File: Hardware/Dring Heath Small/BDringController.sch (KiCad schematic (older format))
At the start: 93 parts, among them J1 Module 1, J10 Module 3, J11 JTAG, J12 Shift Regs and Motor Drvs, J13 Module 4, J14 Module 5, J15 Micro_SD_Card, J16 Pin, J17 Pin, J18 Pin, J19 Pin, J2 Jumper, J20 Pin, J21 Pin, J22 AUX GPIO, J3 Motor, J4 Module 1, J5 Ext Mot Drv, J6 01x02, J7 THC_Display, J8 Module 2, J9 VMot, U1 ESP32_38p, U10 Y, U11 z, U12 A, U13 B, U14 C, U2 74LVC157A, U3 ESP32_38p, U4 TC1262-33, U5 74AHCT595, U6 74AHCT595, U7 74AHCT595, U8 74AHCT595, U9 X

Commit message: Routing
needs 2 Jumper wires 18v in and 15v
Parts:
- added C25: 100nf, Capacitor_SMD:C_0603_1608Metric_Pad1.08x0.95mm_HandSolder, symbol Device:C_Small
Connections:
- net +3V3: now also C25.2
- net GND: now also J6.2 (Pin_2), PS1.2 (-Vin), PS2.2 (-Vin), C25.1
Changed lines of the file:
@@
 $EndComp
 Wire Wire Line
-	11250 2850 11250 3350
-Wire Wire Line
 	11250 3350 11650 3350
-Connection ~ 11650 3350
 Wire Wire Line
 	9950 1950 9950 2450
@@
 	-1   0    0    1
 $EndComp
+$Comp
+L Device:C_Small C25
+U 1 1 6025EA04
+P 5450 1300
+F 0 "C25" V 5500 1050 50  0000 C CNN
+F 1 "100nf" V 5400 1050 50  0000 C CNN
+F 2 "Capacitor_SMD:C_0603_1608Metric_Pad1.08x0.95mm_HandSolder" H 5450 1300 50  0001 C CNN
+F 3 "~" H 5450 1300 50  0001 C CNN
+	1    5450 1300
+	0    -1   -1   0
+$EndComp
+Connection ~ 5350 1300
+Wire Wire Line
+	5550 1300 5900 1300
+Wire Wire Line
+	5900 1300 5900 1400
+Wire Wire Line
+	5900 1400 6050 1400
+Connection ~ 6050 1400
+Connection ~ 11650 3350
+Wire Wire Line
+	11250 2850 11250 3350
+$Comp
+L power:GND #PWR0106
+U 1 1 605E21DB
+P 6250 7100
+F 0 "#PWR0106" H 6250 6850 50  0001 C CNN
+F 1 "GND" H 6255 6927 50  0000 C CNN
+F 2 "" H 6250 7100 50  0001 C CNN
+F 3 "" H 6250 7100 50  0001 C CNN
+	1    6250 7100
+	1    0    0    -1
+$EndComp
+Wire Wire Line
+	6100 7100 6250 7100
 Wire Bus Line
 	9500 1650 9500 5450

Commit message: Main and Module Boards Routed
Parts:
- removed J11: JTAG, Connector_PinHeader_2.54mm:PinHeader_2x05_P2.54mm_Horizontal, symbol Connector:Conn_ARM_JTAG_SWD_10
- added H10, H11, H8, H9: ~, Connector_Pin:Pin_D0.9mm_L10.0mm_W2.4mm_FlatFork, symbol Mechanical:MountingHole_Pad
- renumbered C6 to C1, C14 to C10, C15 to C11, C16 to C12, C17 to C13, C18 to C14, C1 to C15, C19 to C16, C2 to C17, C20 to C18, C3 to C19, C25 to C2, C21 to C20, C4 to C21, C5 to C23, C23 to C24, C24 to C25, C7 to C3, C8 to C4, C9 to C5, C10 to C6, C11 to C7, C12 to C8, C13 to C9, J22 to J1, J8 to J10, J9 to J11, J10 to J12, J12 to J13, J13 to J14, J14 to J15, J15 to J16, J16 to J17, J17 to J18, J18 to J19, J23 to J2, J19 to J20, J20 to J21, J21 to J22, J1 to J3, J2 to J4, J3 to J5, J4 to J6, J5 to J7, J6 to J8, J7 to J9, R21 to R10, R22 to R11, R23 to R12, R16 to R5, R17 to R6, R18 to R7, R19 to R8, R20 to R9
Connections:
- net +15V: now also H11.1
- net at J8.1 (Pin_1), PS1.1 (+Vin), PS2.1 (+Vin): now also H9.1
- no-connect marks 39 -> 41
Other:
- moved on the sheet: C5, C8, D1, J13, U3

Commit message: Pin changes
Put RJ45 connector on Jtag module for more IO put Pot on Torch module to
adjust Plasma voltage
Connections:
- net TCH_V_IO36: now reaches U1.22 (IO36)
- net TCH_V_IO36: now also J12.10 (7)
- net TCHIO17: no longer names the net of U1.9 (IO17)
- net TCHIO17: no longer J12.10 (7)
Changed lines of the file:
@@
 TCHIO21
 Text GLabel 8150 8850 1    39   BiDi ~ 8
-TCHIO17
-Text GLabel 4800 1500 2    39   BiDi ~ 8
-TCHIO22
+TCH_V_IO36
 Text GLabel 4800 1800 2    39   BiDi ~ 8
 TCHIO21
-Text GLabel 4800 2300 2    39   BiDi ~ 8
-TCHIO17
 $Comp
 L power:GND #PWR09
@@
 Wire Wire Line
 	4100 3800 4100 4000
-NoConn ~ 4000 1500
 Text GLabel 4000 1900 0    39   Input ~ 0
 TorchTrigger
@@
 NoConn ~ 3500 5350
 NoConn ~ 3500 5450
+Text GLabel 4000 1500 0    39   BiDi ~ 8
+TCH_V_IO36
+Text GLabel 4800 1500 2    39   BiDi ~ 8
+TCHIO22
+NoConn ~ 4800 2300
 Wire Bus Line
 	9500 1650 9500 5450

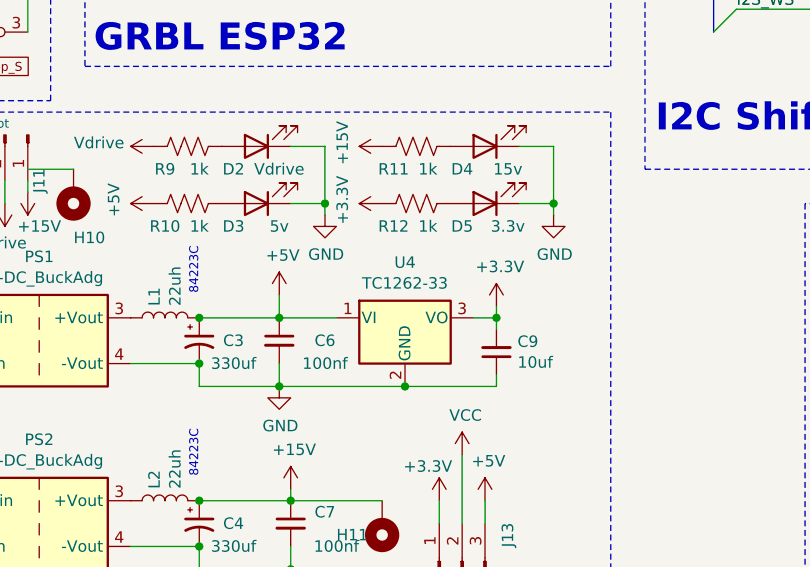
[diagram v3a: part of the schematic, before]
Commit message: Change to BOM
Shifted a few tracks changed 3.3v reg to 1A
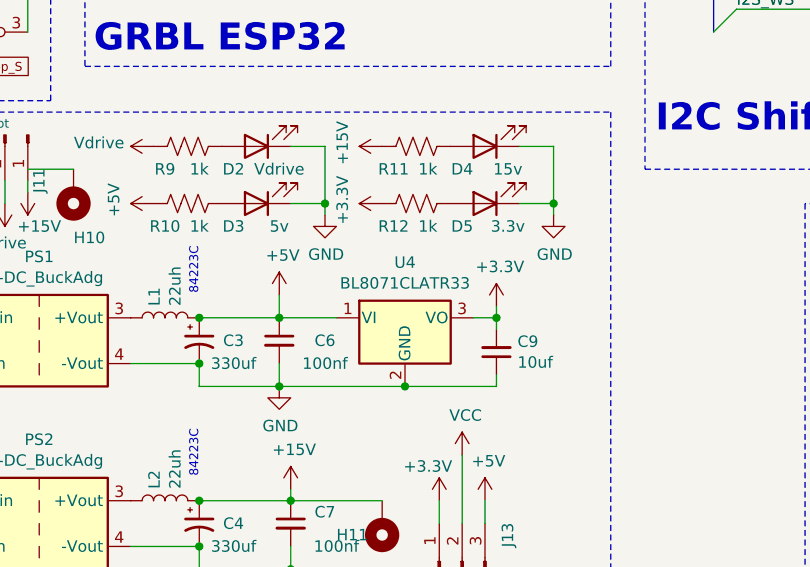
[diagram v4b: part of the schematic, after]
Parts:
- U4: value TC1262-33 -> BL8071CLATR33
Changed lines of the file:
@@
 P 8150 6700
 F 0 "U4" H 8150 6942 50  0000 C CNN
-F 1 "TC1262-33" H 8150 6851 50  0000 C CNN
+F 1 "BL8071CLATR33" H 8150 6851 50  0000 C CNN
 F 2 "Package_TO_SOT_SMD:SOT-223" H 8150 6925 50  0001 C CIN
 F 3 "http://ww1.microchip.com/downloads/en/DeviceDoc/21373C.pdf" H 8150 6400 50  0001 C CNN

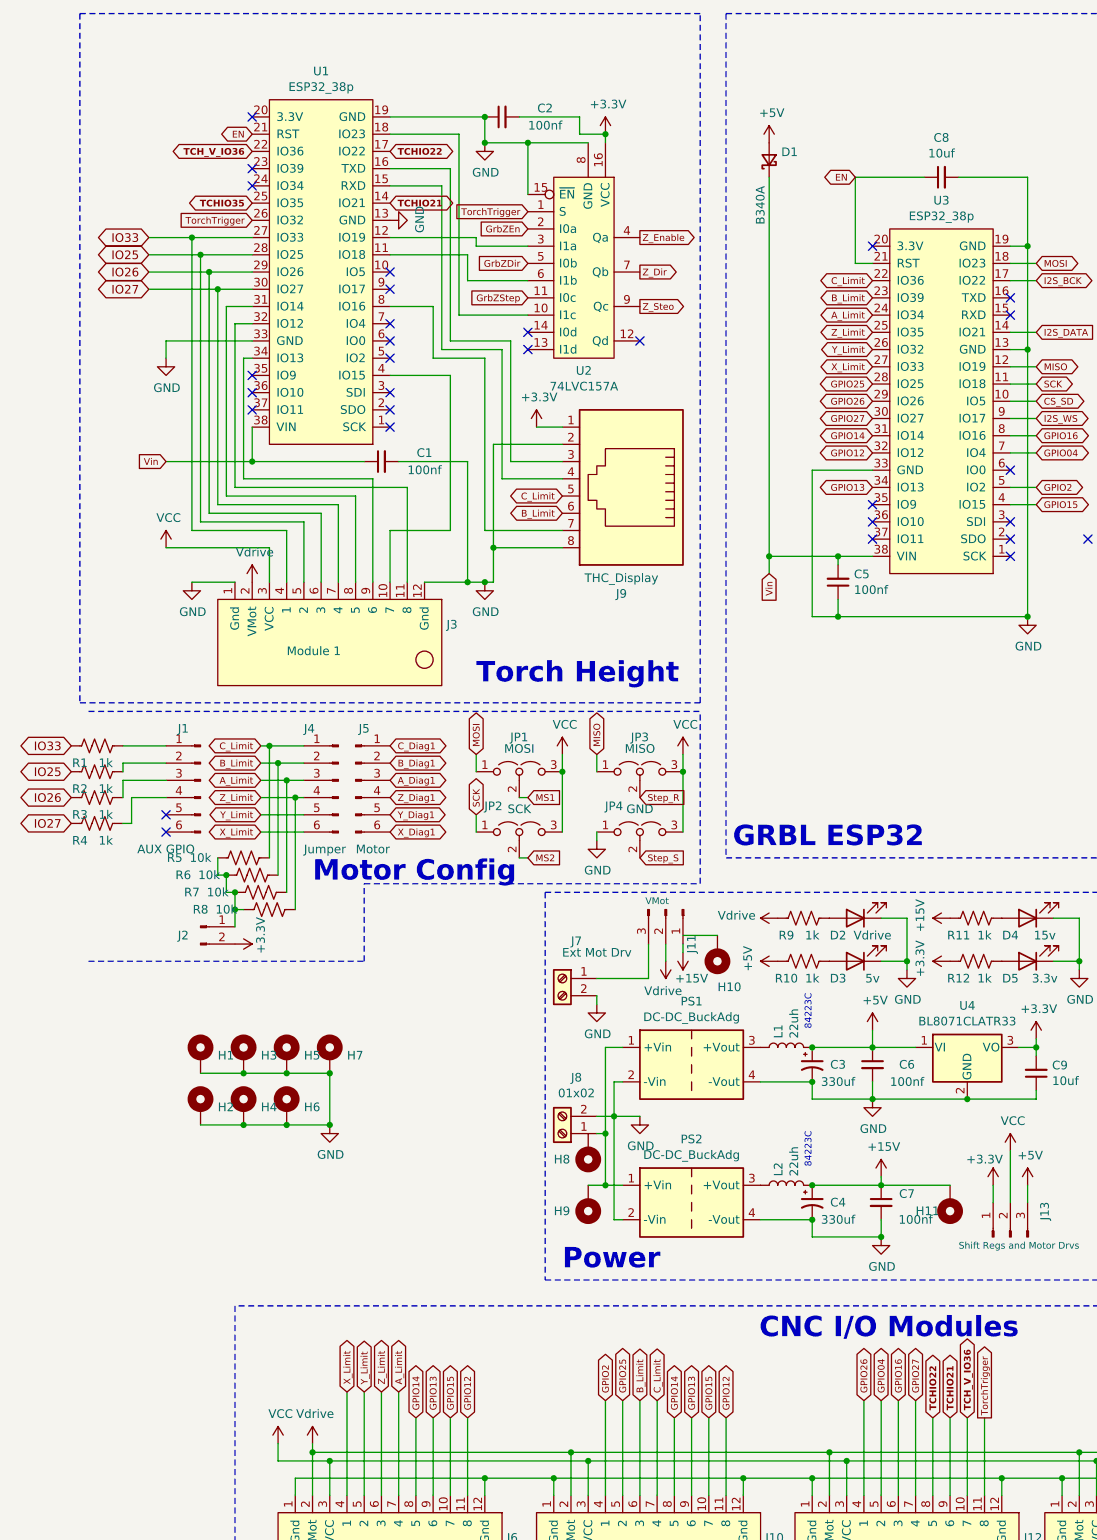
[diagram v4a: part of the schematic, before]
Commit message: Added external A/D ADS1115
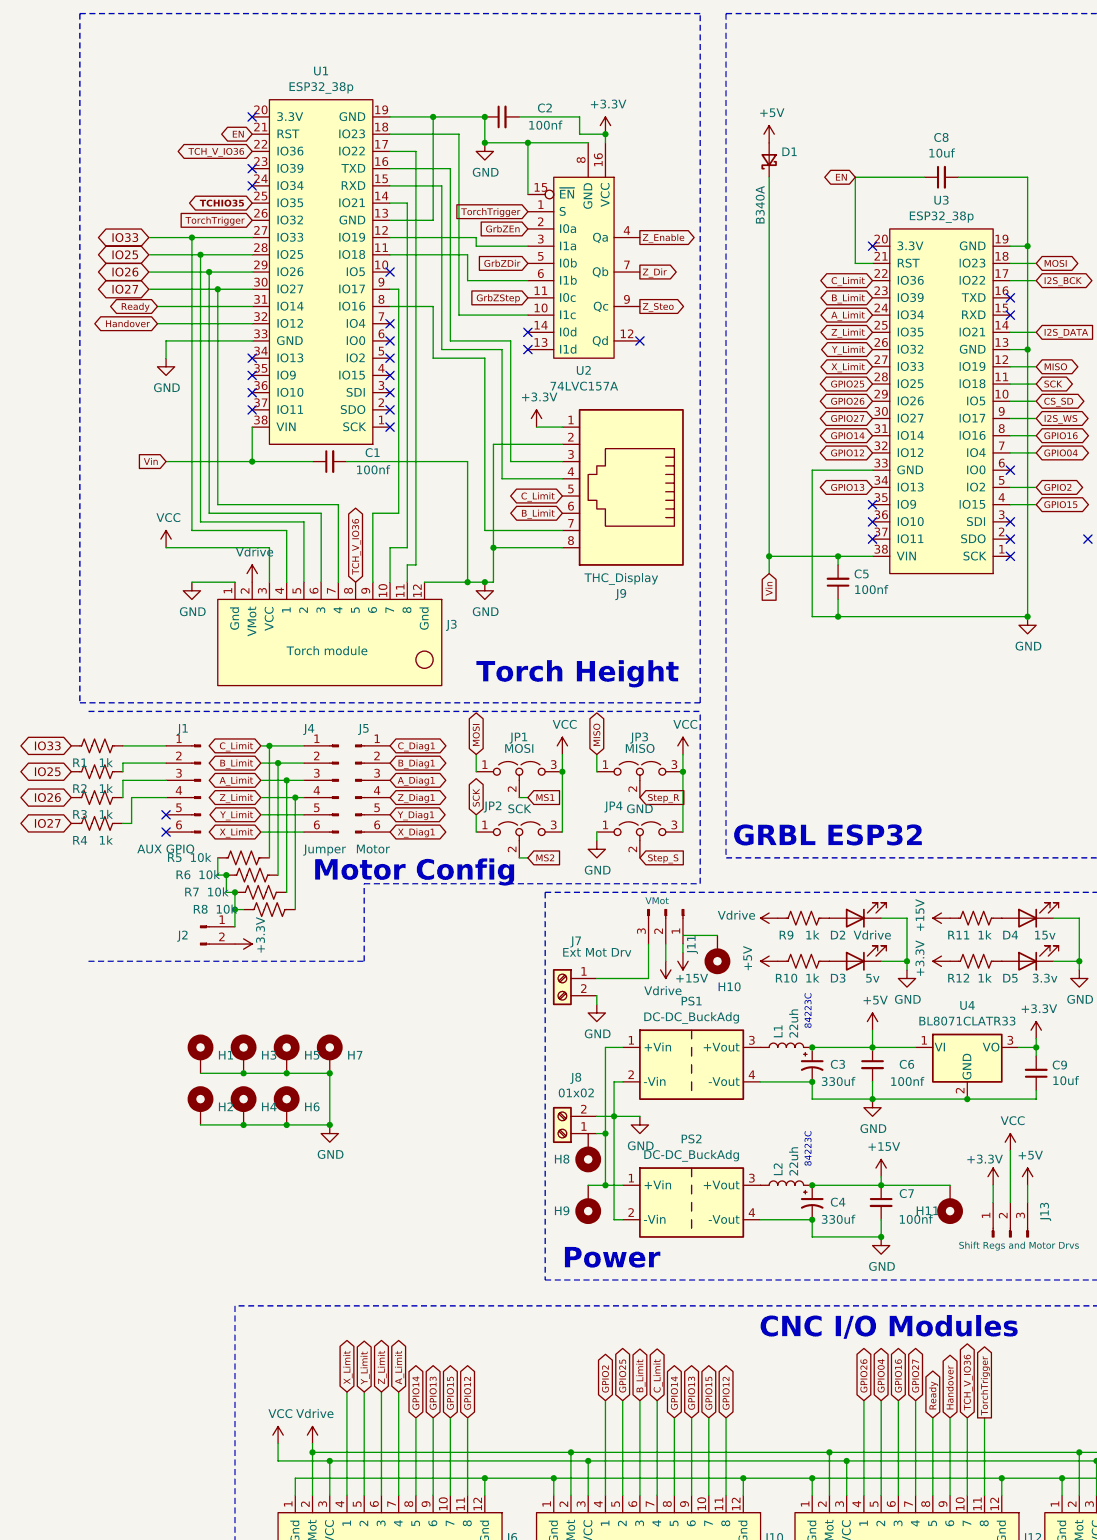
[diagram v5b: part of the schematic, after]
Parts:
- J3: value Module 1 -> Torch module
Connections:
- net TCH_V_IO36: now also J3.8 (5)
- net Ready: now reaches U1.31 (IO14)
- net Ready: now also J12.8 (5); no longer J3.8 (5)
- net at J3.11 (8): now also U1.17 (IO22); no longer U1.32 (IO12)
- net at U1.34 (IO13): no longer J3.9 (6)
- net at J3.10 (7): now also U1.14 (IO21); no longer U1.4 (IO15)
- net at U1.9 (IO17): now also J3.9 (6)
- net TCHIO21 renamed Handover
- net Handover: now also U1.32 (IO12); no longer U1.14 (IO21)
- removed net TCHIO22: J12.8 (5), U1.17 (IO22)
- no-connect marks 41 -> 42
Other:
- moved on the sheet: C1
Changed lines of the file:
@@
 P 4450 4350
 F 0 "J3" H 3772 4246 50  0000 R CNN
-F 1 "Module 1" H 4700 4400 50  0000 R CNN
+F 1 "Torch module" H 4700 4400 50  0000 R CNN
 F 2 "Connector_PinSocket_2.54mm:PinSocket_1x12_P2.54mm_Vertical" H 4350 4300 50  0001 C CNN
 F 3 "" H 4350 4300 50  0001 C CNN
@@
 	-1   0    0    1
 $EndComp
-Wire Wire Line
-	4000 2500 3900 2500
-Wire Wire Line
-	3900 2500 3900 3450
-Wire Wire Line
-	3900 3450 4900 3450
-Wire Wire Line
-	4900 3450 4900 4000
-Wire Wire Line
-	4800 3700 4800 4000
-Wire Wire Line
-	4000 2700 3950 2700
-Wire Wire Line
-	3950 2700 3950 3400
-Wire Wire Line
-	3950 3400 4700 3400
-Wire Wire Line
-	4700 3400 4700 4000
-Wire Wire Line
-	4000 2400 3850 2400
-Wire Wire Line
-	3850 2400 3850 3500
-Wire Wire Line
-	3850 3500 4600 3500
-Wire Wire Line
-	4600 3500 4600 4000
 Wire Wire Line
 	4000 2300 3800 2300
@@
 L Device:C_Small C1
 U 1 1 60B8E4F3
-P 4750 3300
-F 0 "C1" V 4800 3050 50  0000 C CNN
-F 1 "100nf" V 4700 3050 50  0000 C CNN
-F 2 "Capacitor_SMD:C_0603_1608Metric_Pad1.08x0.95mm_HandSolder" H 4750 3300 50  0001 C CNN
-F 3 "~" H 4750 3300 50  0001 C CNN
-	1    4750 3300
+P 4450 3300
+F 0 "C1" V 4500 3050 50  0000 C CNN
+F 1 "100nf" V 4400 3050 50  0000 C CNN
+F 2 "Capacitor_SMD:C_0603_1608Metric_Pad1.08x0.95mm_HandSolder" H 4450 3300 50  0001 C CNN
+F 3 "~" H 4450 3300 50  0001 C CNN
+	1    4450 3300
 	0    -1   -1   0
 $EndComp
@@
 Text GLabel 5600 2350 0    39   Input ~ 0
 GrbZStep
-Wire Wire Line
-	5150 2800 5150 3700
 NoConn ~ 4000 2800
 NoConn ~ 4000 2900
@@
 	3500 2600 3500 2700
 Wire Wire Line
-	4000 3300 4650 3300
+	4000 3300 4350 3300
 Wire Wire Line
 	3500 3300 4000 3300
@@
 	5000 4000 5250 4000
 Wire Wire Line
-	4800 1300 5350 1300
+	4800 1300 5050 1300
 Wire Wire Line
 	4800 1400 5200 1400
@@
 	4800 2400 5050 2400
 Wire Wire Line
-	4800 2800 5150 2800
-Wire Wire Line
-	4850 3300 5250 3300
-Wire Wire Line
-	4800 3700 5150 3700
+	4550 3300 5250 3300
 Wire Wire Line
 	5400 4000 5350 4000
 Connection ~ 5350 4000
-Text GLabel 7950 8850 1    39   BiDi ~ 8
-TCHIO22
-Text GLabel 8050 8850 1    39   BiDi ~ 8
-TCHIO21
-Text GLabel 8150 8850 1    39   BiDi ~ 8
+Text GLabel 7950 8850 1    39   BiDi ~ 0
+Ready
+Text GLabel 8050 8850 1    39   BiDi ~ 0
+Handover
+Text GLabel 8150 8850 1    39   BiDi ~ 0
 TCH_V_IO36
-Text GLabel 4800 1800 2    39   BiDi ~ 8
-TCHIO21
-$Comp
-L power:GND #PWR09
-U 1 1 642F7395
-P 4800 1900
-F 0 "#PWR09" H 4800 1650 50  0001 C CNN
-F 1 "GND" H 4805 1727 50  0000 C CNN
-F 2 "" H 4800 1900 50  0001 C CNN
-F 3 "" H 4800 1900 50  0001 C CNN
-	1    4800 1900
-	0    -1   -1   0
-$EndComp
 NoConn ~ 4800 2500
 NoConn ~ 4800 2600
@@
 NoConn ~ 3500 5350
 NoConn ~ 3500 5450
-Text GLabel 4000 1500 0    39   BiDi ~ 8
+Text GLabel 4000 1500 0    39   BiDi ~ 0
 TCH_V_IO36
-Text GLabel 4800 1500 2    39   BiDi ~ 8
-TCHIO22
-NoConn ~ 4800 2300
+Wire Wire Line
+	3450 2400 4000 2400
+Wire Wire Line
+	3450 2500 4000 2500
+Text GLabel 3450 2400 0    39   BiDi ~ 0
+Ready
+Text GLabel 3450 2500 0    39   BiDi ~ 0
+Handover
+Wire Wire Line
+	4800 1900 5050 1900
+Wire Wire Line
+	5050 1900 5050 1300
+Connection ~ 5050 1300
+Wire Wire Line
+	5050 1300 5350 1300
+Wire Wire Line
+	4850 3600 4700 3600
+Wire Wire Line
+	4700 3600 4700 4000
+Wire Wire Line
+	4800 2300 4850 2300
+Wire Wire Line
+	4850 2300 4850 3600
+Wire Wire Line
+	4800 1800 4900 1800
+Wire Wire Line
+	4900 1800 4900 3800
+Wire Wire Line
+	4900 3800 4800 3800
+Wire Wire Line
+	4800 3800 4800 4000
+Wire Wire Line
+	4800 1500 4950 1500
+Wire Wire Line
+	4950 1500 4950 3900
+Wire Wire Line
+	4950 3900 4900 3900
+Wire Wire Line
+	4900 3900 4900 4000
+NoConn ~ 4800 2800
+Text GLabel 4600 4000 1    39   BiDi ~ 0
+TCH_V_IO36
+NoConn ~ 4000 2700
 Wire Bus Line
 	9500 1650 9500 5450

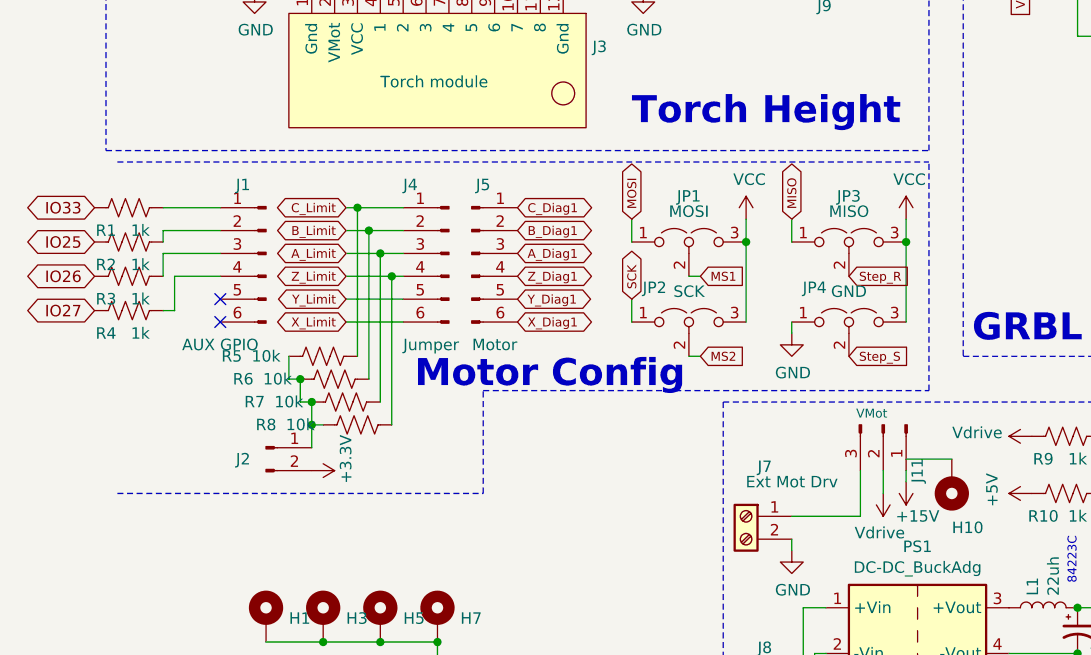
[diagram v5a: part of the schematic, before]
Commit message: routed a/d board
put simulation on excel bom
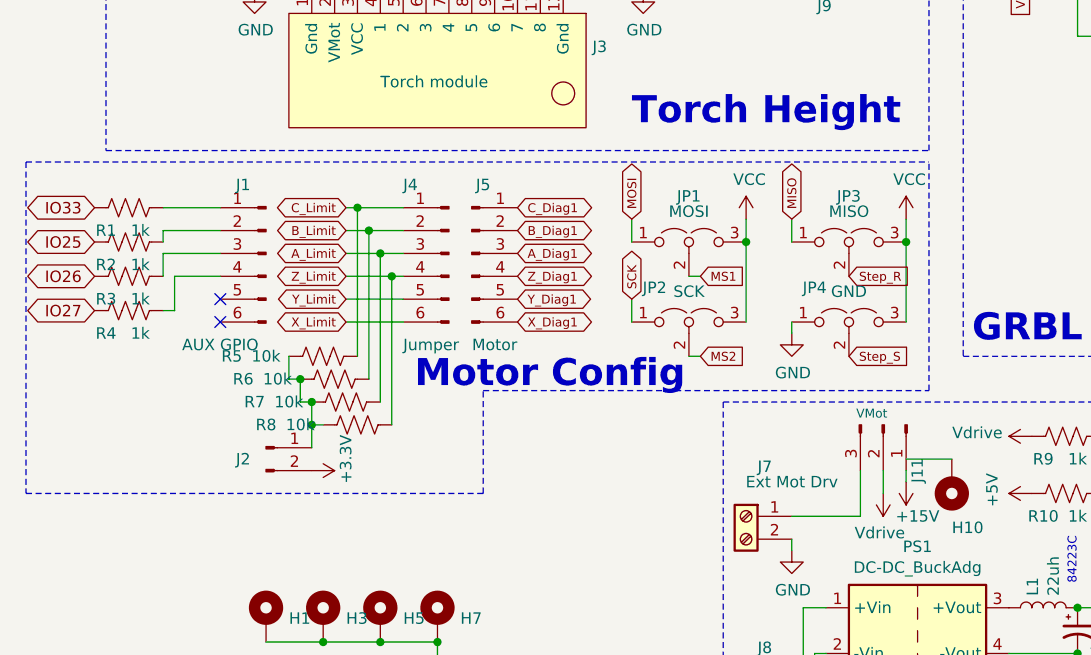
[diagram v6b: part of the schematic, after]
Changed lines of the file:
@@
 	-1   0    0    -1
 $EndComp
-Wire Notes Line
-	3050 4750 6600 4750
-Wire Notes Line
-	3050 6200 4650 6200
 Text GLabel 3400 2000 0    50   BiDi ~ 0
 IO33
@@
 TCH_V_IO36
 NoConn ~ 4000 2700
+Wire Notes Line
+	2650 4750 2650 6200
+Wire Notes Line
+	2650 4750 6600 4750
+Wire Notes Line
+	2650 6200 4650 6200
 Wire Bus Line
 	9500 1650 9500 5450

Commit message: changed reset circuit on ESP 32s and driver board gerber
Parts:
- removed C8: 10uf, Capacitor_SMD:C_0603_1608Metric_Pad1.08x0.95mm_HandSolder, symbol Device:C_Small
- added J23, J24: RST, Connector_PinHeader_2.54mm:PinHeader_1x02_P2.54mm_Vertical, symbol Connector:Conn_01x02_Male
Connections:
- net GND: now also J23.2 (Pin_2), J24.2 (Pin_2)
- net EN: no longer names the net of U3.21 (RST)
- net EN: now also J24.1 (Pin_1); no longer U1.21 (RST)
- new net: J23.1 (Pin_1), U1.21 (RST)
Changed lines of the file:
@@
 	8500 2050 8500 2650
 Connection ~ 8500 2650
-$Comp
-L Device:C_Small C8
-U 1 1 6036FDC2
-P 8000 1650
-F 0 "C8" V 8229 1650 50  0000 C CNN
-F 1 "10uf" V 8138 1650 50  0000 C CNN
-F 2 "Capacitor_SMD:C_0603_1608Metric_Pad1.08x0.95mm_HandSolder" H 8000 1650 50  0001 C CNN
-F 3 "~" H 8000 1650 50  0001 C CNN
-	1    8000 1650
-	0    -1   -1   0
-$EndComp
 Wire Wire Line
 	7600 2150 7500 2150
-Wire Wire Line
-	7500 2150 7500 1650
-Wire Wire Line
-	7500 1650 7900 1650
-Wire Wire Line
-	8100 1650 8500 1650
-Wire Wire Line
-	8500 1650 8500 2050
-Connection ~ 8500 2050
 Text GLabel 7600 2750 0    39   BiDi ~ 0
 X_Limit
@@
 Text GLabel 8550 3250 2    39   BiDi ~ 0
 GPIO04
-Text GLabel 7500 1650 0    39   BiDi ~ 0
-EN
 Text GLabel 8550 3450 2    39   BiDi ~ 0
 GPIO2
@@
 	14900 3700 14900 3800
 Connection ~ 14900 3700
-Text GLabel 4000 1400 0    39   BiDi ~ 0
-EN
 $Comp
 L Connector:Conn_01x06_Male J1
@@
 Wire Notes Line
 	2650 6200 4650 6200
+$Comp
+L Connector:Conn_01x02_Male J23
+U 1 1 602DB20F
+P 3650 1000
+F 0 "J23" H 3550 950 50  0000 C CNN
+F 1 "RST" H 3758 1090 50  0000 C CNN
+F 2 "Connector_PinHeader_2.54mm:PinHeader_1x02_P2.54mm_Vertical" H 3650 1000 50  0001 C CNN
+F 3 "~" H 3650 1000 50  0001 C CNN
+	1    3650 1000
+	0    1    1    0
+$EndComp
+$Comp
+L Connector:Conn_01x02_Male J24
+U 1 1 602DFFF8
+P 7500 1300
+F 0 "J24" H 7400 1250 50  0000 C CNN
+F 1 "RST" H 7608 1390 50  0000 C CNN
+F 2 "Connector_PinHeader_2.54mm:PinHeader_1x02_P2.54mm_Vertical" H 7500 1300 50  0001 C CNN
+F 3 "~" H 7500 1300 50  0001 C CNN
+	1    7500 1300
+	0    1    1    0
+$EndComp
+$Comp
+L power:GND #PWR09
+U 1 1 603B4B58
+P 3550 1300
+F 0 "#PWR09" H 3550 1050 50  0001 C CNN
+F 1 "GND" H 3555 1127 50  0000 C CNN
+F 2 "" H 3550 1300 50  0001 C CNN
+F 3 "" H 3550 1300 50  0001 C CNN
+	1    3550 1300
+	1    0    0    -1
+$EndComp
+$Comp
+L power:GND #PWR055
+U 1 1 603B606B
+P 7400 1600
+F 0 "#PWR055" H 7400 1350 50  0001 C CNN
+F 1 "GND" H 7405 1427 50  0000 C CNN
+F 2 "" H 7400 1600 50  0001 C CNN
+F 3 "" H 7400 1600 50  0001 C CNN
+	1    7400 1600
+	1    0    0    -1
+$EndComp
+Wire Wire Line
+	7500 1500 7500 2150
+Wire Wire Line
+	7400 1600 7400 1500
+Wire Wire Line
+	4000 1400 3650 1400
+Wire Wire Line
+	3650 1400 3650 1200
+Wire Wire Line
+	3550 1300 3550 1200
 Wire Bus Line
 	9500 1650 9500 5450
